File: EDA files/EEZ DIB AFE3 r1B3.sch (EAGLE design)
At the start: 148 parts, among them IC1 AMC3330QDWERQ1, IC11 ADS131E04IPAGR, IC12 TPS71725DCKR, IC13 TPS72325DBVR, IC2 ULN2803ADWR, IC3 AMC3301DWER, IC4 MCP6004T-I/ST, IC5 DG212BDY-T1-E3, IC6 MCP6001T-I/OT, IC7 DG212BDY-T1-E3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

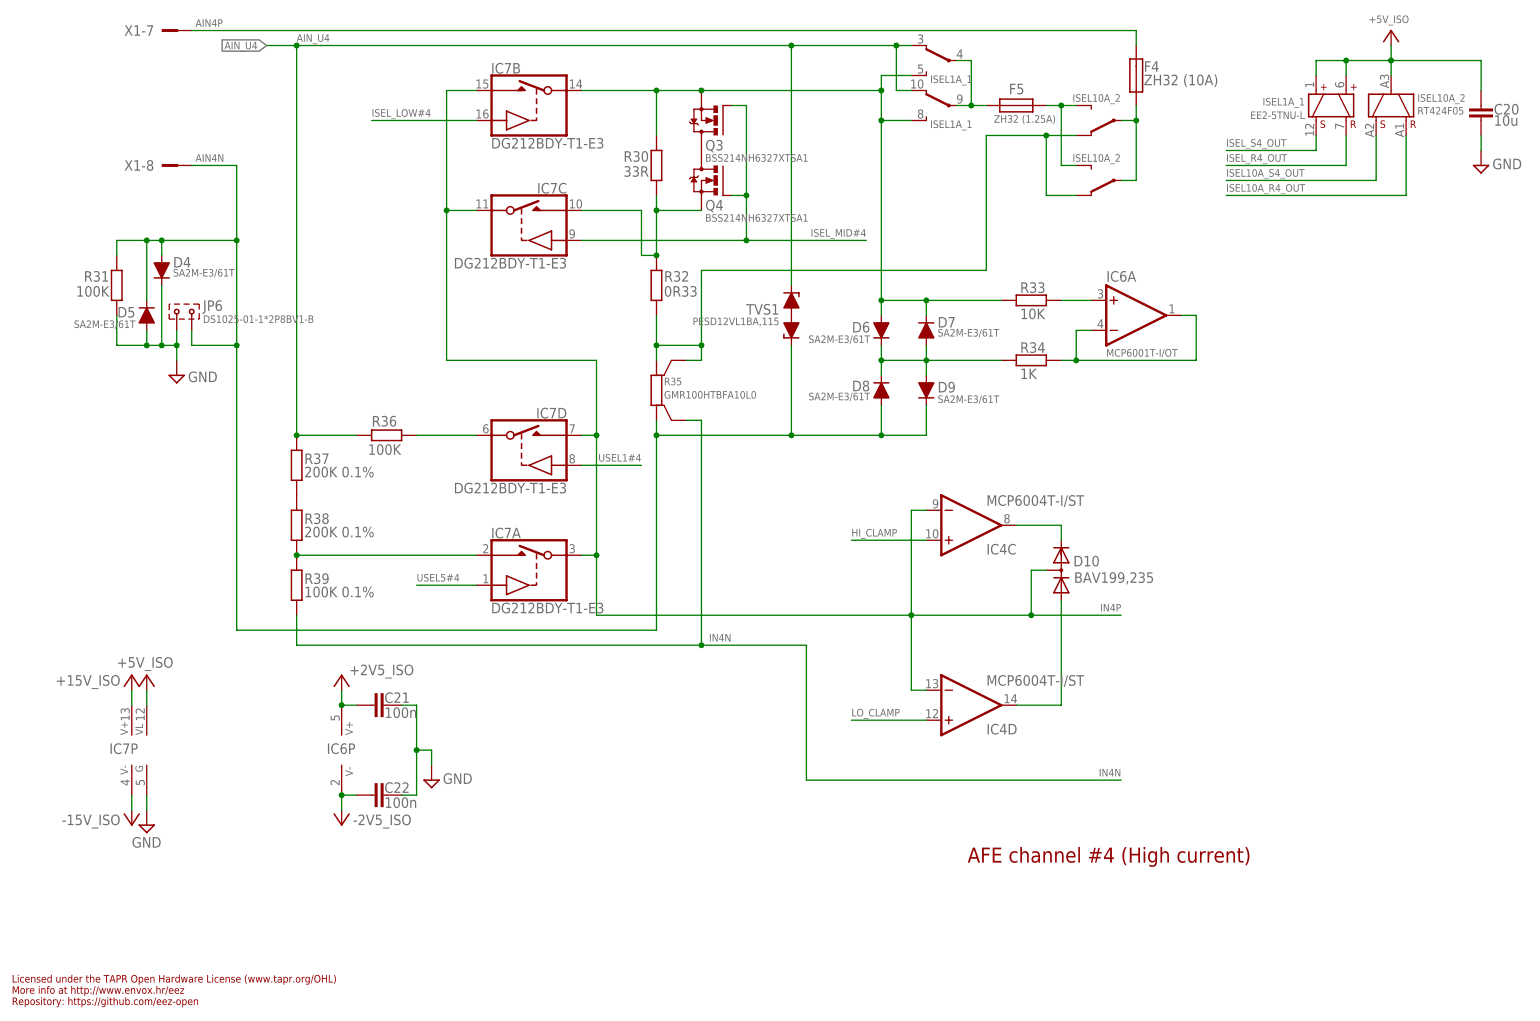
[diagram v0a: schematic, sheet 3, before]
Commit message: New Rsense values, PCB layout adjustment for mid range Rsense
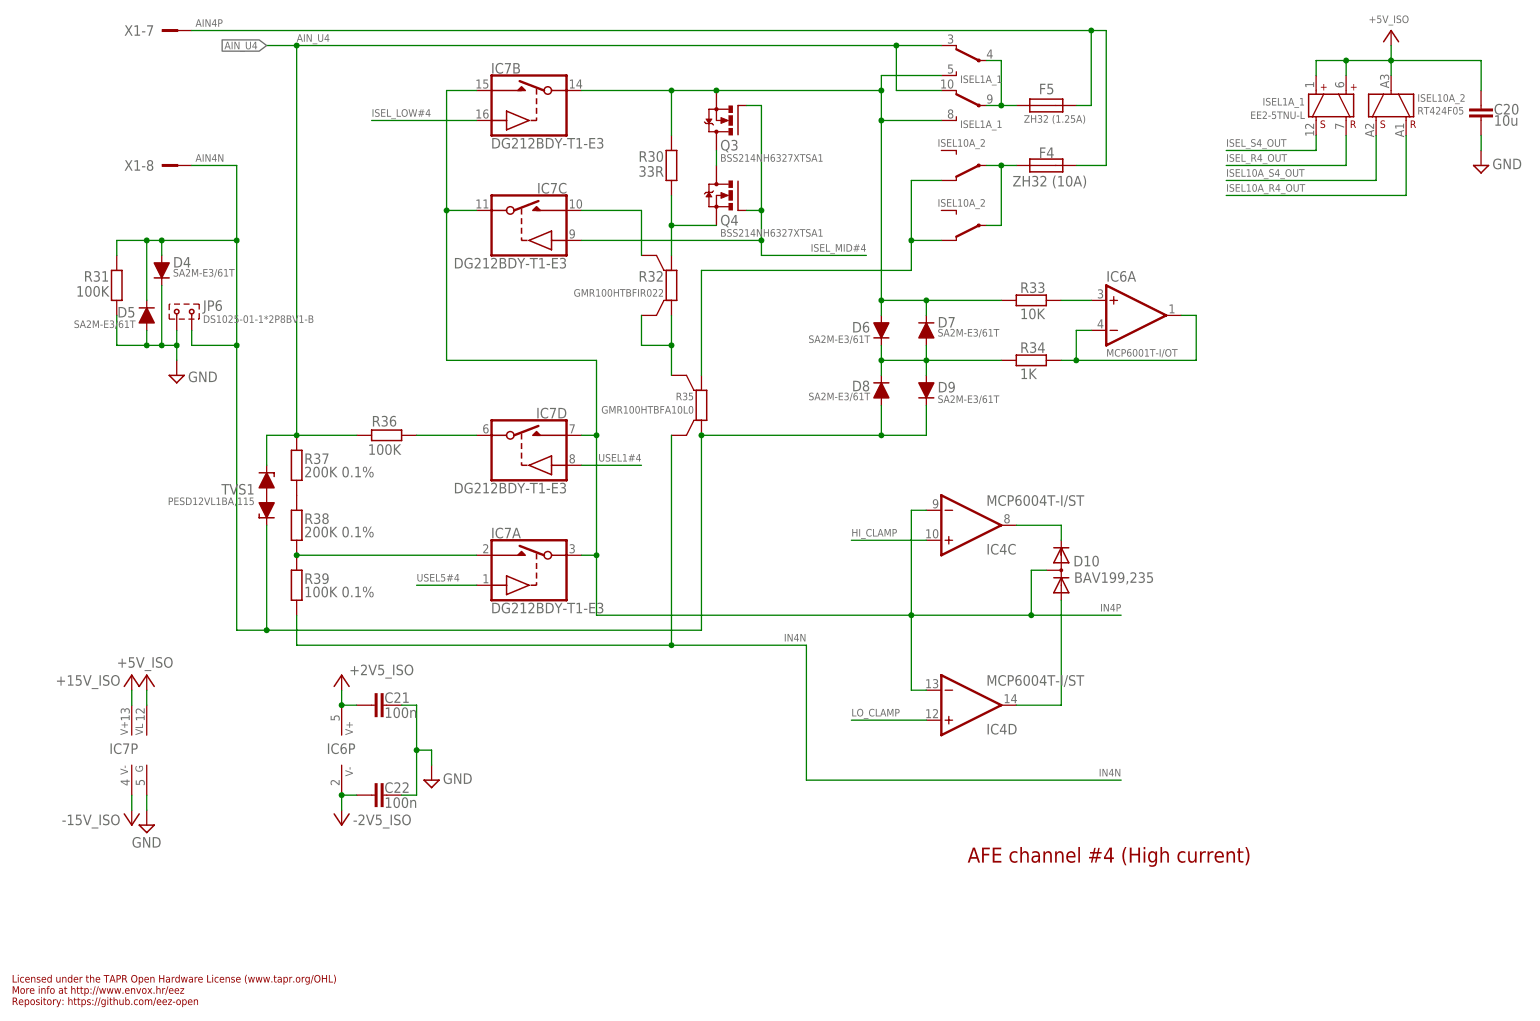
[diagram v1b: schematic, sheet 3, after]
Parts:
- R13: value 15R -> 10R
- R15: value 50R 0.1% -> 33R 0.1%
- R32: value 0R33 -> GMR100HTBFIR022; device rcl:R-EU_R1210 -> EEZ_Lib1:R-EU_4WIRE2512
- R8: value 0R220 -> GMR100HTBFIR022; device rcl:R-EU_R1210 -> EEZ_Lib1:R-EU_4WIRE2512
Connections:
- net N$18 renamed HI_SENSE+
- removed net N$141: F5.2, ISEL10A_2B.NO, ISEL10A_2C.NO
- removed net N$71: F2.2, ISEL10A_1C.NO, R8.2
- new net HI_FORCE+: ISEL10A_1B.NC, R11.2, R8.1, R8.1S
- new net LOW_SENSE+: ISEL10A_1C.NO, R8.2S
- new net LO_FORCE-: F2.2, R8.2
- new net N$27: IC7C.D, R32.2S
- net AIN4P: now also F5.2
- net HI_CURR#1: no longer R32.1, R35.2S
- net ISEL#3: now also X3-15.1
- net N$170: no longer IC7C.D
- net N$19: now also R32.1, R32.1S, R35.2S; no longer ISEL10A_1B.NC, R11.2, R8.1
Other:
- note added: "Dovesti na ADIB AIN1 i AIN2 !!!"
- moved on the sheet: F4, F5, ISEL10A_2, ISEL1A_1, Q3, Q4, R11, R30, R35, TVS1

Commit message: R30 value corrected
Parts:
- R30: value 33R -> 20R
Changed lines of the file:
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@@
 <part name="R32" library="EEZ_Lib1" deviceset="R-EU_4WIRE" device="2512" value="GMR100HTBFIR022"/>
 <part name="F5" library="EEZ_Lib1" deviceset="ZH32" device="" value="ZH32 (1.25A)"/>
-<part name="R30" library="rcl" deviceset="R-EU_" device="R1206" value="33R"/>
+<part name="R30" library="rcl" deviceset="R-EU_" device="R1206" value="20R"/>
 <part name="R33" library="rcl" deviceset="R-EU_" device="R0805" value="10K"/>
 <part name="D6" library="EEZ_DIB" deviceset="DIODE" device="_SMA-NARROW" value="SA2M-E3/61T"/>
@@
 <wire x1="170.18" y1="121.92" x2="157.48" y2="121.92" width="0.1524" layer="91"/>
 <junction x="157.48" y="121.92"/>
-<wire x1="99.06" y1="157.48" x2="114.3" y2="157.48" width="0.1524" layer="91"/>
-<junction x="114.3" y="157.48"/>
+<wire x1="99.06" y1="157.48" x2="111.76" y2="157.48" width="0.1524" layer="91"/>
 <pinref part="Q3" gate="A" pin="S"/>
 <junction x="121.92" y="157.48"/>
@@
 <pinref part="ISEL1A_1" gate="C" pin="NO"/>
 <pinref part="IC7" gate="B" pin="S"/>
-</segment>
-</net>
+<wire x1="114.3" y1="149.86" x2="111.76" y2="149.86" width="0.1524" layer="91"/>
+<wire x1="111.76" y1="149.86" x2="111.76" y2="157.48" width="0.1524" layer="91"/>
+<junction x="114.3" y="149.86"/>
+</segment>
+</net>
